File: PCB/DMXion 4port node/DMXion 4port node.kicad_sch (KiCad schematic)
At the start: 12 parts

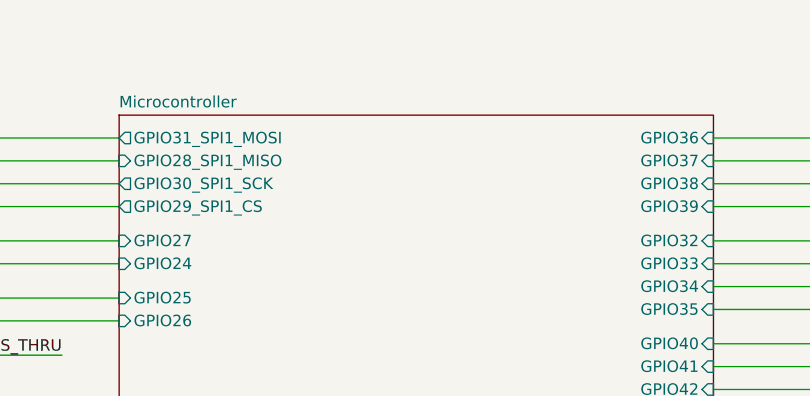
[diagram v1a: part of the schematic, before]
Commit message: Even more testpads
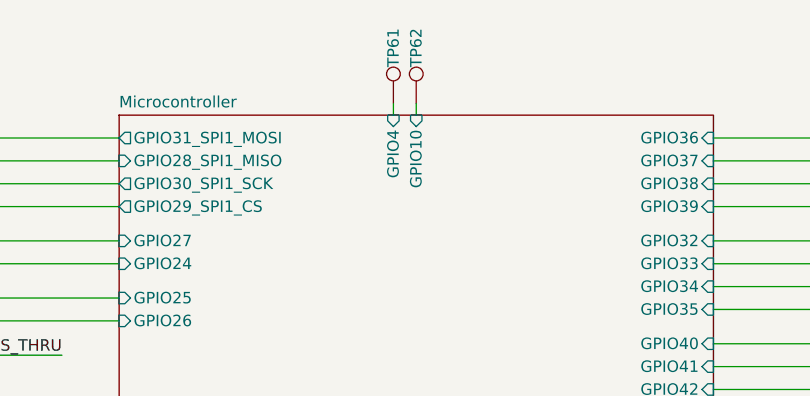
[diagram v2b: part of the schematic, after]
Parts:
- added TP61, TP62: TestPoint, TestPoint:TestPoint_Pad_D1.5mm, symbol Connector:TestPoint
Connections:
- new net Microcontroller/GPIO10: TP62.1
- new net Microcontroller/GPIO4: TP61.1
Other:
- sheet Microcontroller ports: added GPIO10, GPIO4; removed none
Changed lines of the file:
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@@
+	(wire
+		(pts
+			(xy 139.7 26.67) (xy 139.7 27.94)
+		)
+		(stroke
+			(width 0)
+			(type default)
+		)
+	)
 	(wire
 		(pts
@@
 		(pts
 			(xy 91.44 104.14) (xy 109.22 104.14)
+		)
+		(stroke
+			(width 0)
+			(type default)
+		)
+	)
+	(wire
+		(pts
+			(xy 142.24 26.67) (xy 142.24 27.94)
 		)
 		(stroke
@@
 	)
 	(symbol
+		(lib_id "Connector:TestPoint")
+		(at 142.24 26.67 0)
+		(unit 1)
+		(body_style 1)
+		(exclude_from_sim no)
+		(in_bom yes)
+		(on_board yes)
+		(in_pos_files yes)
+		(dnp no)
+		(property "Reference" "TP62"
+			(at 142.24 22.606 90)
+			(show_name no)
+			(do_not_autoplace no)
+			(effects
+				(font
+					(size 1.27 1.27)
+				)
+				(justify left)
+			)
+		)
+		(property "Value" "TestPoint"
+			(at 144.78 24.6379 0)
+			(hide yes)
+			(show_name no)
+			(do_not_autoplace no)
+			(effects
+				(font
+					(size 1.27 1.27)
+				)
+				(justify left)
+			)
+		)
+		(property "Footprint" "TestPoint:TestPoint_Pad_D1.5mm"
+			(at 147.32 26.67 0)
+			(hide yes)
+			(show_name no)
+			(do_not_autoplace no)
+			(effects
+				(font
+					(size 1.27 1.27)
+				)
+			)
+		)
+		(property "Datasheet" ""
+			(at 147.32 26.67 0)
+			(hide yes)
+			(show_name no)
+			(do_not_autoplace no)
+			(effects
+				(font
+					(size 1.27 1.27)
+				)
+			)
+		)
+		(property "Description" "test point"
+			(at 142.24 26.67 0)
+			(hide yes)
+			(show_name no)
+			(do_not_autoplace no)
+			(effects
+				(font
+					(size 1.27 1.27)
+				)
+			)
+		)
+		(pin "1"
+		)
+		(instances
+			(project "DMXion 4port node"
+				(path "/7d5b1976-98b3-4e47-ae52-3fe360235ea3"
+					(reference "TP62")
+					(unit 1)
+				)
+			)
+		)
+	)
+	(symbol
 		(lib_id "Mechanical:Fiducial")
 		(at 76.2 171.45 0)
@@
 	)
 	(symbol
+		(lib_id "Connector:TestPoint")
+		(at 139.7 26.67 0)
+		(unit 1)
+		(body_style 1)
+		(exclude_from_sim no)
+		(in_bom yes)
+		(on_board yes)
+		(in_pos_files yes)
+		(dnp no)
+		(property "Reference" "TP61"
+			(at 139.7 22.606 90)
+			(show_name no)
+			(do_not_autoplace no)
+			(effects
+				(font
+					(size 1.27 1.27)
+				)
+				(justify left)
+			)
+		)
+		(property "Value" "TestPoint"
+			(at 142.24 24.6379 0)
+			(hide yes)
+			(show_name no)
+			(do_not_autoplace no)
+			(effects
+				(font
+					(size 1.27 1.27)
+				)
+				(justify left)
+			)
+		)
+		(property "Footprint" "TestPoint:TestPoint_Pad_D1.5mm"
+			(at 144.78 26.67 0)
+			(hide yes)
+			(show_name no)
+			(do_not_autoplace no)
+			(effects
+				(font
+					(size 1.27 1.27)
+				)
+			)
+		)
+		(property "Datasheet" ""
+			(at 144.78 26.67 0)
+			(hide yes)
+			(show_name no)
+			(do_not_autoplace no)
+			(effects
+				(font
+					(size 1.27 1.27)
+				)
+			)
+		)
+		(property "Description" "test point"
+			(at 139.7 26.67 0)
+			(hide yes)
+			(show_name no)
+			(do_not_autoplace no)
+			(effects
+				(font
+					(size 1.27 1.27)
+				)
+			)
+		)
+		(pin "1"
+		)
+		(instances
+			(project "DMXion 4port node"
+				(path "/7d5b1976-98b3-4e47-ae52-3fe360235ea3"
+					(reference "TP61")
+					(unit 1)
+				)
+			)
+		)
+	)
+	(symbol
 		(lib_id "Mechanical:MountingHole")
 		(at 91.44 177.8 0)
@@
 			(effects
 				(font
+					(size 1.27 1.27)
+				)
+				(justify right)
+			)
+		)
+		(pin "GPIO4" input
+			(at 139.7 27.94 90)
+			(effects
+				(font
+					(size 1.27 1.27)
+				)
+				(justify right)
+			)
+		)
+		(pin "GPIO10" input
+			(at 142.24 27.94 90)
+			(effects
+				(font
